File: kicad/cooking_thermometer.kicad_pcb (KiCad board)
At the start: 2 copper layers, 88.9 x 50.8 mm, 40 parts, among them J1 FTDI, J2 STLINK, J3 3V3_Power, J4 Battery, J6 OLED_CONN, J7 USB_B_Micro, J8 THERMO_CONN, Q1 BC547, SW1 BOOT0_SW, SW2 NRST_SW, SW3 UI_A_SW, SW4 UI_B_SW, SW5 UI_C_SW, U1 STM32F070F6Px, U2 MCP1700x-330xxTO, U3 MCP73831-2-OT

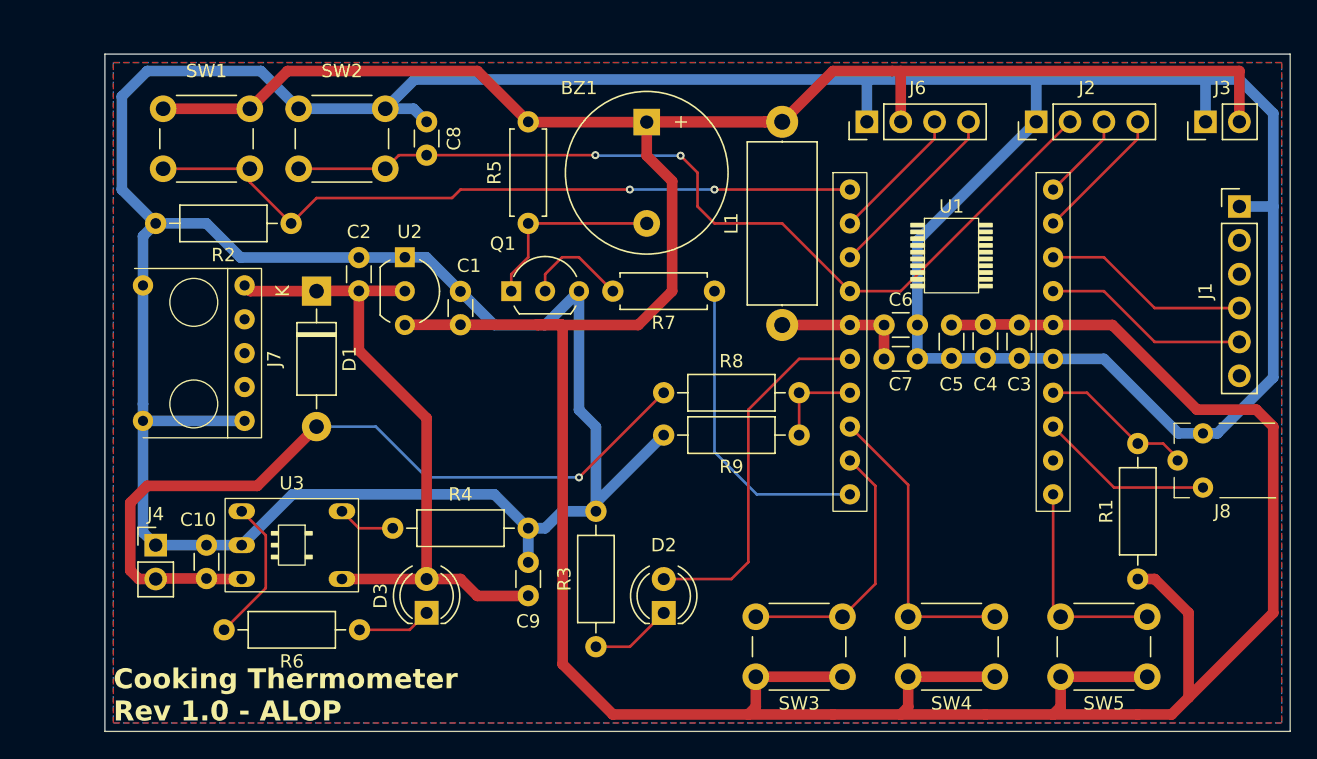
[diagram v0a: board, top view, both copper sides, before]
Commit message: Edit schematic for nrf52810
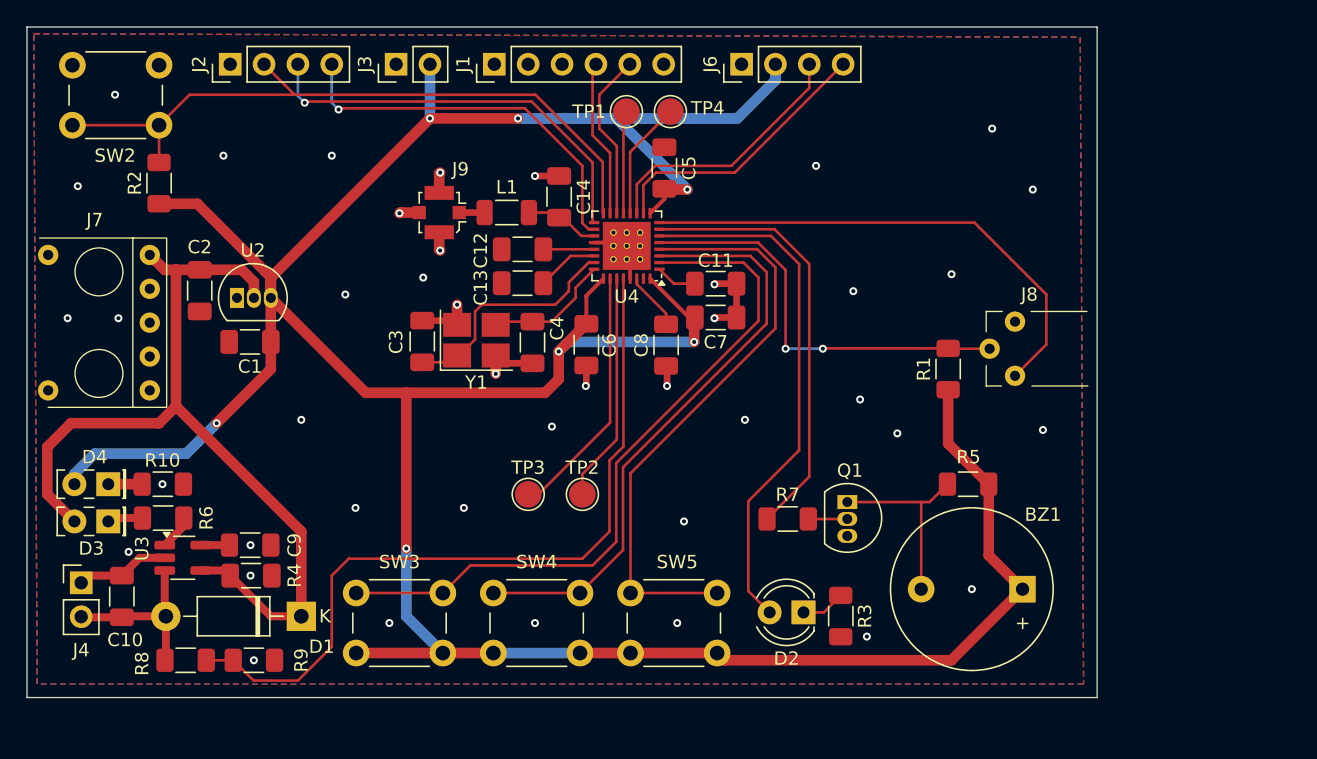
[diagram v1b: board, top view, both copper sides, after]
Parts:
- removed SW1: BOOT0_SW, Button_Switch_THT:SW_PUSH_6mm
- removed U1: STM32F070F6Px, MyOwnFootprintLibrary:STM32F070_DIP20
- added C11: 100nF, Capacitor_SMD:C_1206_3216Metric_Pad1.33x1.80mm_HandSolder, F.Cu at (139.8, 97.2)
- added C12: NC, Capacitor_SMD:C_1206_3216Metric_Pad1.33x1.80mm_HandSolder, F.Cu at (125.3, 94.7)
- added C13: 100pF, Capacitor_SMD:C_1206_3216Metric_Pad1.33x1.80mm_HandSolder, F.Cu at (125.3, 97.2)
- added C14: 0.8pF, Capacitor_SMD:C_1206_3216Metric_Pad1.33x1.80mm_HandSolder, F.Cu at (128.0, 90.7)
- added D4: GREEN_LED_PWR, LED_THT:LED_Rectangular_W5.0mm_H2.0mm, F.Cu at (94.2, 112.3)
- added J9: Conn_Coaxial, Connector_Coaxial:U.FL_Molex_MCRF_73412-0110_Vertical, F.Cu at (119.1, 91.9)
- added R10: 330, Resistor_SMD:R_1206_3216Metric_Pad1.30x1.75mm_HandSolder, F.Cu at (98.3, 112.3)
- added TP1: P0.16, TestPoint:TestPoint_Pad_D2.0mm, F.Cu at (133.1, 84.3)
- added TP2: P0.28, TestPoint:TestPoint_Pad_D2.0mm, F.Cu at (129.8, 113.0)
- added TP3: P0.25, TestPoint:TestPoint_Pad_D2.0mm, F.Cu at (125.7, 113.0)
- added TP4: P0.15, TestPoint:TestPoint_Pad_D2.0mm, F.Cu at (136.4, 84.3)
- added U4: nRF52810-QCxx, Package_DFN_QFN:QFN-32-1EP_5x5mm_P0.5mm_EP3.6x3.6mm_ThermalVias, F.Cu at (133.1, 94.4)
- added Y1: 32MHz, Crystal:Crystal_SMD_3225-4Pin_3.2x2.5mm_HandSoldering, F.Cu at (121.8, 101.5)
- C1, C10, C2, C5, C9: footprint Capacitor_THT:C_Disc_D3.0mm_W1.6mm_P2.50mm -> Capacitor_SMD:C_1206_3216Metric_Pad1.33x1.80mm_HandSolder
- C3: value 4.7uF -> 12pF; footprint Capacitor_THT:C_Disc_D3.0mm_W1.6mm_P2.50mm -> Capacitor_SMD:C_1206_3216Metric_Pad1.33x1.80mm_HandSolder
- C4: value 100nF -> 12pF; footprint Capacitor_THT:C_Disc_D3.0mm_W1.6mm_P2.50mm -> Capacitor_SMD:C_1206_3216Metric_Pad1.33x1.80mm_HandSolder
- C6: value 1uF -> 100nF; footprint Capacitor_THT:C_Disc_D3.0mm_W1.6mm_P2.50mm -> Capacitor_SMD:C_1206_3216Metric_Pad1.33x1.80mm_HandSolder
- C7: value 10nF -> 4.7uF; footprint Capacitor_THT:C_Disc_D3.0mm_W1.6mm_P2.50mm -> Capacitor_SMD:C_1206_3216Metric_Pad1.33x1.80mm_HandSolder
- C8: value 100nF -> 1uF; footprint Capacitor_THT:C_Disc_D3.0mm_W1.6mm_P2.50mm -> Capacitor_SMD:C_1206_3216Metric_Pad1.33x1.80mm_HandSolder
- D3: footprint LED_THT:LED_D4.0mm -> LED_THT:LED_Rectangular_W5.0mm_H2.0mm
- L1: value 680nH -> 3.9nH; footprint Inductor_THT:L_Axial_L12.0mm_D5.0mm_P15.24mm_Horizontal_Fastron_MISC -> Inductor_SMD:L_1206_3216Metric_Pad1.22x1.90mm_HandSolder
- Q1: footprint Package_TO_SOT_THT:TO-92L_Inline_Wide -> Package_TO_SOT_THT:TO-92L_Inline
- R1, R2, R3, R4, R6, R8, R9: footprint Resistor_THT:R_Axial_DIN0207_L6.3mm_D2.5mm_P10.16mm_Horizontal -> Resistor_SMD:R_1206_3216Metric_Pad1.30x1.75mm_HandSolder
- R5, R7: footprint Resistor_THT:R_Axial_DIN0207_L6.3mm_D2.5mm_P7.62mm_Horizontal -> Resistor_SMD:R_1206_3216Metric_Pad1.30x1.75mm_HandSolder
- U2: footprint Package_TO_SOT_THT:TO-92_Inline_Wide -> Package_TO_SOT_THT:TO-92L_Inline
- U3: footprint MyOwnFootprintLibrary:DIP-5-6_7.62mm_5on6 -> Package_TO_SOT_SMD:SOT-23-5_HandSoldering
- moved J3 60.9 mm to (115.8, 80.8)
- moved J2 60.6 mm to (103.4, 80.8)
- moved J1 56.9 mm to (123.2, 80.8), turned to 90 degrees
- moved BZ1 45.0 mm to (162.8, 120.1), turned to 180 degrees
- moved C3 44.8 mm to (117.8, 101.6)
- moved R9 44.2 mm to (105.2, 125.5), turned to 0 degrees
- moved R5 42.7 mm to (158.7, 112.3), turned to 180 degrees
- moved R8 41.1 mm to (100.0, 125.5)
- moved C4 34.0 mm to (126.0, 101.6)
- moved SW5 32.3 mm to (139.9, 124.9)
- moved SW4 31.2 mm to (129.6, 124.9)
- moved SW3 30.0 mm to (119.3, 124.9)
- moved Q1 29.8 mm to (149.7, 113.6), turned to -90 degrees
- moved D3 24.8 mm to (94.2, 115.1), turned to 180 degrees
- moved C8 24.6 mm to (136.1, 101.8), turned to 90 degrees
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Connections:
- net /ADC1_BATT_MEAS renamed /ADC_BATT_MEAS
- net /ADC9_TEMP_MEAS renamed /ADC_TEMP_MEAS
- C3 pad 1: +3.3V -> GND
- C3 pad 2: GND -> Net-(U4-XC1)
- C4 pad 1: +3.3V -> Net-(U4-XC2)
- C5 pad 1: +3.3V -> GND
- C5 pad 2: GND -> +3.3V
- C6 pad 1: Net-(U1-VDDA) -> GND
- C6 pad 2: GND -> +3.3V
- C7 pad 1: Net-(U1-VDDA) -> GND
- C7 pad 2: GND -> +3.3V
- C8 pad 2: /NRST -> Net-(U4-DEC4)
- L1 pad 1: +3.3V -> /RF
- L1 pad 2: Net-(U1-VDDA) -> /ANT
- R2 pad 1: Net-(U1-BOOT0) -> +3.3V
- R2 pad 2: GND -> /NRST
- R7 pad 1: /TIM14_CH1_BUZZER_PWM -> /BUZZER_PWM
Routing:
- net GND: track 320.6 -> 34.0 mm, vias 0 -> 42
- net +3.3V: track 305.9 -> 239.7 mm, vias 0 -> 7
- net Net-(U1-BOOT0): track 54.8 -> 0.00 mm, vias 2 -> 0
- net /ADC_BATT_MEAS: track 6.98 -> 58.0 mm
- net +BATT: track 60.3 -> 13.2 mm, vias 1 -> 0
- net /UI_A: track 20.0 -> 53.2 mm
- net /BUZZER_PWM: track 0.00 -> 32.8 mm
- net /UI_C: track 15.9 -> 44.7 mm
- net /~{JACK_CONNECTED}: track 13.1 -> 38.3 mm
- net /SWCLK: track 6.66 -> 31.2 mm, vias 0 -> 1
- net /TIM14_CH1_BUZZER_PWM: track 23.5 -> 0.00 mm
- net /UI_B: track 22.6 -> 44.9 mm
- net /ADC_TEMP_MEAS: track 11.6 -> 31.5 mm, vias 0 -> 2
- net Net-(U4-P0.25): track 0.00 -> 19.2 mm
- net /SWDIO: track 10.3 -> 29.1 mm, vias 0 -> 1
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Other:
- board size 88.9 x 50.8 mm -> 80.3 x 50.3 mm
- board text removed: "Cooking Thermometer Rev 1.0 - ALOP"
